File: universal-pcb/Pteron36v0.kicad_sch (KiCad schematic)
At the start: 64 parts, among them J1 AudioJack4, J2 AudioJack4, J3 Conn_01x04, SW10 SW_PUSH, SW12 SW_PUSH, SW13 SW_PUSH, SW14 SW_PUSH, SW15 SW_PUSH, SW17 SW_PUSH, SW18 SW_PUSH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

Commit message: super is ready
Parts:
- added LOGO? (x2): LOGO-OTL, personal-logo:peacock-medium, symbol SparkFun-Aesthetics:LOGO-OTL
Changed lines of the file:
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@@
+    )
+  )
+  (symbol (lib_id "SparkFun-Aesthetics:LOGO-OTL") (at 252.73 76.2 0) (unit 1)
+    (in_bom yes) (on_board yes)
+    (property "Reference" "LOGO?" (id 0) (at 252.73 76.2 0)
+      (effects (font (size 1.27 1.27)) hide)
+    )
+    (property "Value" "LOGO-OTL" (id 1) (at 252.73 76.2 0)
+      (effects (font (size 1.27 1.27)) hide)
+    )
+    (property "Footprint" "personal-logo:peacock-medium" (id 2) (at 253.492 72.39 0)
+      (effects (font (size 0.508 0.508)) hide)
+    )
+    (property "Datasheet" "" (id 3) (at 252.73 76.2 0)
+      (effects (font (size 1.27 1.27)) hide)
+    )
+  )
+  (symbol (lib_id "SparkFun-Aesthetics:LOGO-OTL") (at 252.73 86.36 0) (unit 1)
+    (in_bom yes) (on_board yes)
+    (property "Reference" "LOGO?" (id 0) (at 252.73 86.36 0)
+      (effects (font (size 1.27 1.27)) hide)
+    )
+    (property "Value" "LOGO-OTL" (id 1) (at 252.73 86.36 0)
+      (effects (font (size 1.27 1.27)) hide)
+    )
+    (property "Footprint" "personal-logo:peacock-medium" (id 2) (at 253.492 82.55 0)
+      (effects (font (size 0.508 0.508)) hide)
+    )
+    (property "Datasheet" "" (id 3) (at 252.73 86.36 0)
+      (effects (font (size 1.27 1.27)) hide)
     )
   )
@@
       (reference "LOGO2") (unit 1) (value "LOGO-OTL") (footprint "personal-logo:miryoku-kicad-small")
     )
+    (path "/a9b58b6f-e7ea-4927-95e3-e75d74487149"
+      (reference "LOGO?") (unit 1) (value "LOGO-OTL") (footprint "personal-logo:peacock-medium")
+    )
+    (path "/f6a143f1-2ae8-4506-91d2-2bed25c6d340"
+      (reference "LOGO?") (unit 1) (value "LOGO-OTL") (footprint "personal-logo:peacock-medium")
+    )
     (path "/00000000-0000-0000-0000-0000607d063e"

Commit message: verify gerber
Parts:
- gave numbers to parts that had none: 2
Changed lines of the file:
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@@
   (symbol (lib_id "SparkFun-Aesthetics:LOGO-OTL") (at 252.73 76.2 0) (unit 1)
     (in_bom yes) (on_board yes)
-    (property "Reference" "LOGO?" (id 0) (at 252.73 76.2 0)
+    (property "Reference" "LOGO3" (id 0) (at 252.73 76.2 0)
       (effects (font (size 1.27 1.27)) hide)
     )
@@
   (symbol (lib_id "SparkFun-Aesthetics:LOGO-OTL") (at 252.73 86.36 0) (unit 1)
     (in_bom yes) (on_board yes)
-    (property "Reference" "LOGO?" (id 0) (at 252.73 86.36 0)
+    (property "Reference" "LOGO4" (id 0) (at 252.73 86.36 0)
       (effects (font (size 1.27 1.27)) hide)
     )
@@
     )
     (path "/a9b58b6f-e7ea-4927-95e3-e75d74487149"
-      (reference "LOGO?") (unit 1) (value "LOGO-OTL") (footprint "personal-logo:peacock-medium")
+      (reference "LOGO3") (unit 1) (value "LOGO-OTL") (footprint "personal-logo:peacock-medium")
     )
     (path "/f6a143f1-2ae8-4506-91d2-2bed25c6d340"
-      (reference "LOGO?") (unit 1) (value "LOGO-OTL") (footprint "personal-logo:peacock-medium")
+      (reference "LOGO4") (unit 1) (value "LOGO-OTL") (footprint "personal-logo:peacock-medium")
     )
     (path "/00000000-0000-0000-0000-0000607d063e"

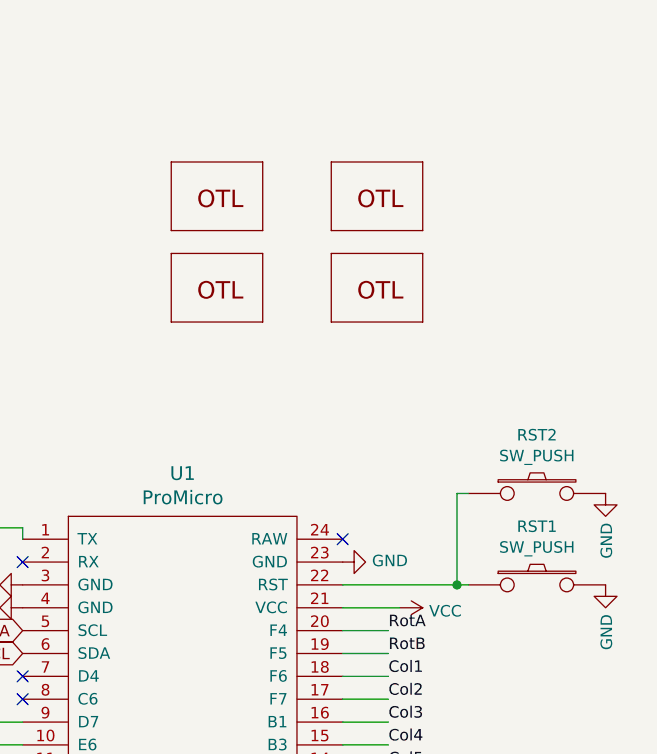
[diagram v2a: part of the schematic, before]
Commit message: introduce the snapable pcb with 4 config of keyboard possible
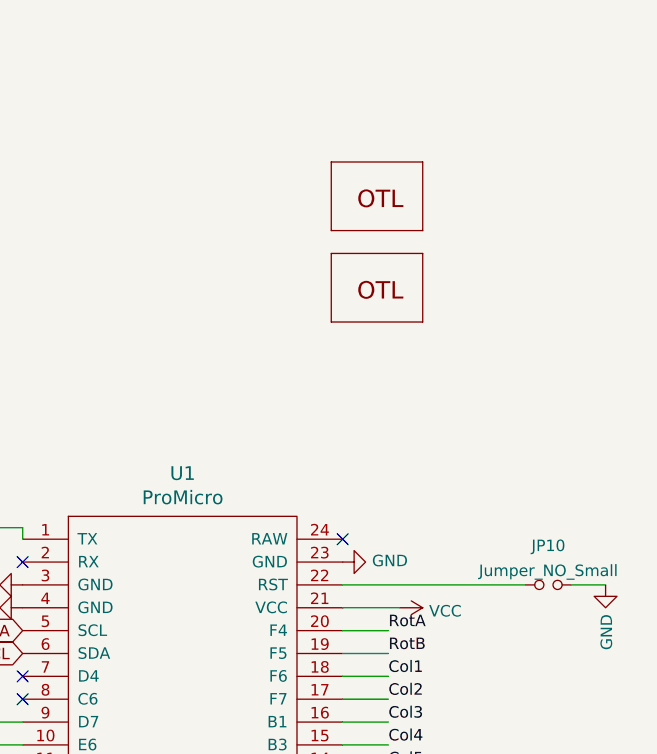
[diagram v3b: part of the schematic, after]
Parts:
- removed LOGO1, LOGO2: LOGO-OTL, personal-logo:miryoku-kicad-small, symbol SparkFun-Aesthetics:LOGO-OTL
- removed RST1, RST2: SW_PUSH, acheron_Hardware:smdPushBtn, symbol keyboard_parts:SW_PUSH
- added JP10: Jumper_NO_Small, User-Submitted:solder_jumper, symbol Device:Jumper_NO_Small
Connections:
- net GND: now also JP10.2
- net at U1.22 (RST): now also JP10.1
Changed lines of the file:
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@@
   (junction (at 107.95 152.4) (diameter 1.016) (color 0 0 0 0))
   (junction (at 119.38 77.47) (diameter 1.016) (color 0 0 0 0))
-  (junction (at 261.62 120.65) (diameter 1.016) (color 0 0 0 0))
   (no_connect (at 213.36 118.11))
   (no_connect (at 213.36 130.81))
@@
     (stroke (width 0) (type solid) (color 0 0 0 0))
   )
-  (wire (pts (xy 248.92 120.65) (xy 261.62 120.65))
+  (wire (pts (xy 248.92 120.65) (xy 269.24 120.65))
     (stroke (width 0) (type solid) (color 0 0 0 0))
   )
@@
     (stroke (width 0) (type solid) (color 0 0 0 0))
   )
-  (wire (pts (xy 261.62 110.49) (xy 262.89 110.49))
-    (stroke (width 0) (type solid) (color 0 0 0 0))
-  )
-  (wire (pts (xy 261.62 120.65) (xy 261.62 110.49))
-    (stroke (width 0) (type solid) (color 0 0 0 0))
-  )
-  (wire (pts (xy 261.62 120.65) (xy 262.89 120.65))
+  (wire (pts (xy 274.32 120.65) (xy 278.13 120.65))
     (stroke (width 0) (type solid) (color 0 0 0 0))
   )
@@
     (pin "2")
   )
+  (symbol (lib_id "Device:Jumper_NO_Small") (at 271.78 120.65 0) (unit 1)
+    (in_bom yes) (on_board yes) (fields_autoplaced)
+    (property "Reference" "JP10" (id 0) (at 271.78 116.3024 0))
+    (property "Value" "Jumper_NO_Small" (id 1) (at 271.78 119.0775 0))
+    (property "Footprint" "User-Submitted:solder_jumper" (id 2) (at 271.78 120.65 0)
+      (effects (font (size 1.27 1.27)) hide)
+    )
+    (property "Datasheet" "~" (id 3) (at 271.78 120.65 0)
+      (effects (font (size 1.27 1.27)) hide)
+    )
+    (pin "1")
+    (pin "2")
+  )
   (symbol (lib_id "power:GND") (at 83.82 144.78 270) (unit 1)
     (in_bom yes) (on_board yes)
@@
     )
     (property "Datasheet" "" (id 3) (at 248.92 118.11 0)
-      (effects (font (size 1.27 1.27)) hide)
-    )
-    (pin "1")
-  )
-  (symbol (lib_id "power:GND") (at 278.13 110.49 0) (unit 1)
-    (in_bom yes) (on_board yes)
-    (property "Reference" "#PWR0118" (id 0) (at 278.13 116.84 0)
-      (effects (font (size 1.27 1.27)) hide)
-    )
-    (property "Value" "GND" (id 1) (at 278.257 113.7412 90)
-      (effects (font (size 1.27 1.27)) (justify right))
-    )
-    (property "Footprint" "" (id 2) (at 278.13 110.49 0)
-      (effects (font (size 1.27 1.27)) hide)
-    )
-    (property "Datasheet" "" (id 3) (at 278.13 110.49 0)
       (effects (font (size 1.27 1.27)) hide)
     )
@@
     (pin "2")
   )
-  (symbol (lib_id "keyboard_parts:SW_PUSH") (at 270.51 110.49 0) (unit 1)
-    (in_bom yes) (on_board yes)
-    (property "Reference" "RST2" (id 0) (at 270.51 104.013 0))
-    (property "Value" "SW_PUSH" (id 1) (at 270.51 106.3244 0))
-    (property "Footprint" "acheron_Hardware:smdPushBtn" (id 2) (at 270.51 110.49 0)
-      (effects (font (size 1.524 1.524)) hide)
-    )
-    (property "Datasheet" "" (id 3) (at 270.51 110.49 0)
-      (effects (font (size 1.524 1.524)))
-    )
-    (pin "1")
-    (pin "2")
-  )
-  (symbol (lib_id "keyboard_parts:SW_PUSH") (at 270.51 120.65 0) (unit 1)
-    (in_bom yes) (on_board yes)
-    (property "Reference" "RST1" (id 0) (at 270.51 114.173 0))
-    (property "Value" "SW_PUSH" (id 1) (at 270.51 116.4844 0))
-    (property "Footprint" "acheron_Hardware:smdPushBtn" (id 2) (at 270.51 120.65 0)
-      (effects (font (size 1.524 1.524)) hide)
-    )
-    (property "Datasheet" "" (id 3) (at 270.51 120.65 0)
-      (effects (font (size 1.524 1.524)))
-    )
-    (pin "1")
-    (pin "2")
-  )
   (symbol (lib_id "Connector_Generic:Conn_01x03") (at 220.98 153.67 0) (unit 1)
     (in_bom yes) (on_board yes)
@@
     (pin "3")
     (pin "4")
-  )
-  (symbol (lib_id "SparkFun-Aesthetics:LOGO-OTL") (at 234.95 76.2 0) (unit 1)
-    (in_bom yes) (on_board yes)
-    (property "Reference" "LOGO1" (id 0) (at 234.95 76.2 0)
-      (effects (font (size 1.27 1.27)) hide)
-    )
-    (property "Value" "LOGO-OTL" (id 1) (at 234.95 76.2 0)
-      (effects (font (size 1.27 1.27)) hide)
-    )
-    (property "Footprint" "personal-logo:miryoku-kicad-small" (id 2) (at 235.712 72.39 0)
-      (effects (font (size 0.508 0.508)) hide)
-    )
-    (property "Datasheet" "" (id 3) (at 234.95 76.2 0)
-      (effects (font (size 1.27 1.27)) hide)
-    )
-  )
-  (symbol (lib_id "SparkFun-Aesthetics:LOGO-OTL") (at 234.95 86.36 0) (unit 1)
-    (in_bom yes) (on_board yes)
-    (property "Reference" "LOGO2" (id 0) (at 234.95 86.36 0)
-      (effects (font (size 1.27 1.27)) hide)
-    )
-    (property "Value" "LOGO-OTL" (id 1) (at 234.95 86.36 0)
-      (effects (font (size 1.27 1.27)) hide)
-    )
-    (property "Footprint" "personal-logo:miryoku-kicad-small" (id 2) (at 235.712 82.55 0)
-      (effects (font (size 0.508 0.508)) hide)
-    )
-    (property "Datasheet" "" (id 3) (at 234.95 86.36 0)
-      (effects (font (size 1.27 1.27)) hide)
-    )
   )
   (symbol (lib_id "SparkFun-Aesthetics:LOGO-OTL") (at 252.73 76.2 0) (unit 1)
@@
       (reference "#PWR0117") (unit 1) (value "VCC") (footprint "")
     )
-    (path "/00000000-0000-0000-0000-0000607e5c9b"
-      (reference "#PWR0118") (unit 1) (value "GND") (footprint "")
-    )
     (path "/00000000-0000-0000-0000-0000607efd8b"
       (reference "#PWR0119") (unit 1) (value "GND") (footprint "")
@@
       (reference "JP8") (unit 1) (value "Jumper_NO_Small") (footprint "SparkFun-Passives:PAD-JUMPER-2-NO_NO_SILK")
     )
-    (path "/00000000-0000-0000-0000-0000607a2bee"
-      (reference "LOGO1") (unit 1) (value "LOGO-OTL") (footprint "personal-logo:miryoku-kicad-small")
-    )
-    (path "/00000000-0000-0000-0000-0000607a2653"
-      (reference "LOGO2") (unit 1) (value "LOGO-OTL") (footprint "personal-logo:miryoku-kicad-small")
+    (path "/cf361c86-9d9b-4dea-a5c2-ea10f53cb6ec"
+      (reference "JP10") (unit 1) (value "Jumper_NO_Small") (footprint "User-Submitted:solder_jumper")
     )
     (path "/a9b58b6f-e7ea-4927-95e3-e75d74487149"
@@
       (reference "RE1") (unit 1) (value "Rotary_Encoder_Switch") (footprint "Rotary_Encoder:RotaryEncoder_Alps_EC11E-Switch_Vertical_H20mm")
     )
-    (path "/00000000-0000-0000-0000-0000607b81a2"
-      (reference "RST1") (unit 1) (value "SW_PUSH") (footprint "acheron_Hardware:smdPushBtn")
-    )
-    (path "/00000000-0000-0000-0000-0000607e0b2f"
-      (reference "RST2") (unit 1) (value "SW_PUSH") (footprint "acheron_Hardware:smdPushBtn")
-    )
     (path "/00000000-0000-0000-0000-000060963566"

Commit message: almost ready final super pcb
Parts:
- JP10: footprint User-Submitted:solder_jumper -> User-Submitted:SolderJumper-flip-2_P1.3mm_Open_Pad1.0x1.5mm
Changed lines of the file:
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@@
     (property "Reference" "JP10" (id 0) (at 271.78 116.3024 0))
     (property "Value" "Jumper_NO_Small" (id 1) (at 271.78 119.0775 0))
-    (property "Footprint" "User-Submitted:solder_jumper" (id 2) (at 271.78 120.65 0)
+    (property "Footprint" "User-Submitted:SolderJumper-flip-2_P1.3mm_Open_Pad1.0x1.5mm" (id 2) (at 271.78 120.65 0)
       (effects (font (size 1.27 1.27)) hide)
     )
@@
     )
     (path "/cf361c86-9d9b-4dea-a5c2-ea10f53cb6ec"
-      (reference "JP10") (unit 1) (value "Jumper_NO_Small") (footprint "User-Submitted:solder_jumper")
+      (reference "JP10") (unit 1) (value "Jumper_NO_Small") (footprint "User-Submitted:SolderJumper-flip-2_P1.3mm_Open_Pad1.0x1.5mm")
     )
     (path "/a9b58b6f-e7ea-4927-95e3-e75d74487149"

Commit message: updated pcb
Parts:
- H1, H2, H3, H4, H5, H6: footprint MountingHole:MountingHole_2.2mm_M2 -> MountingHole:MountingHole_2.2mm_M2_Pad
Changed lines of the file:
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@@
       (effects (font (size 1.27 1.27)) (justify left))
     )
-    (property "Footprint" "MountingHole:MountingHole_2.2mm_M2" (id 2) (at 127 167.64 0)
+    (property "Footprint" "MountingHole:MountingHole_2.2mm_M2_Pad" (id 2) (at 127 167.64 0)
       (effects (font (size 1.27 1.27)) hide)
     )
@@
       (effects (font (size 1.27 1.27)) (justify left))
     )
-    (property "Footprint" "MountingHole:MountingHole_2.2mm_M2" (id 2) (at 127 173.99 0)
+    (property "Footprint" "MountingHole:MountingHole_2.2mm_M2_Pad" (id 2) (at 127 173.99 0)
       (effects (font (size 1.27 1.27)) hide)
     )
@@
       (effects (font (size 1.27 1.27)) (justify left))
     )
-    (property "Footprint" "MountingHole:MountingHole_2.2mm_M2" (id 2) (at 133.35 167.64 0)
+    (property "Footprint" "MountingHole:MountingHole_2.2mm_M2_Pad" (id 2) (at 133.35 167.64 0)
       (effects (font (size 1.27 1.27)) hide)
     )
@@
       (effects (font (size 1.27 1.27)) (justify left))
     )
-    (property "Footprint" "MountingHole:MountingHole_2.2mm_M2" (id 2) (at 133.35 173.99 0)
+    (property "Footprint" "MountingHole:MountingHole_2.2mm_M2_Pad" (id 2) (at 133.35 173.99 0)
       (effects (font (size 1.27 1.27)) hide)
     )
@@
       (effects (font (size 1.27 1.27)) (justify left))
     )
-    (property "Footprint" "MountingHole:MountingHole_2.2mm_M2" (id 2) (at 139.7 167.64 0)
+    (property "Footprint" "MountingHole:MountingHole_2.2mm_M2_Pad" (id 2) (at 139.7 167.64 0)
       (effects (font (size 1.27 1.27)) hide)
     )
@@
       (effects (font (size 1.27 1.27)) (justify left))
     )
-    (property "Footprint" "MountingHole:MountingHole_2.2mm_M2" (id 2) (at 139.7 173.99 0)
+    (property "Footprint" "MountingHole:MountingHole_2.2mm_M2_Pad" (id 2) (at 139.7 173.99 0)
       (effects (font (size 1.27 1.27)) hide)
     )
@@
     )
     (path "/00000000-0000-0000-0000-000060e75eb4"
-      (reference "H1") (unit 1) (value "MountingHole") (footprint "MountingHole:MountingHole_2.2mm_M2")
+      (reference "H1") (unit 1) (value "MountingHole") (footprint "MountingHole:MountingHole_2.2mm_M2_Pad")
     )
     (path "/00000000-0000-0000-0000-000060e7da87"
-      (reference "H2") (unit 1) (value "MountingHole") (footprint "MountingHole:MountingHole_2.2mm_M2")
+      (reference "H2") (unit 1) (value "MountingHole") (footprint "MountingHole:MountingHole_2.2mm_M2_Pad")
     )
     (path "/00000000-0000-0000-0000-000060e77f07"
-      (reference "H3") (unit 1) (value "MountingHole") (footprint "MountingHole:MountingHole_2.2mm_M2")
+      (reference "H3") (unit 1) (value "MountingHole") (footprint "MountingHole:MountingHole_2.2mm_M2_Pad")
     )
     (path "/00000000-0000-0000-0000-000060e7e592"
-      (reference "H4") (unit 1) (value "MountingHole") (footprint "MountingHole:MountingHole_2.2mm_M2")
+      (reference "H4") (unit 1) (value "MountingHole") (footprint "MountingHole:MountingHole_2.2mm_M2_Pad")
     )
     (path "/00000000-0000-0000-0000-000060e7815c"
-      (reference "H5") (unit 1) (value "MountingHole") (footprint "MountingHole:MountingHole_2.2mm_M2")
+      (reference "H5") (unit 1) (value "MountingHole") (footprint "MountingHole:MountingHole_2.2mm_M2_Pad")
     )
     (path "/00000000-0000-0000-0000-000060e7e974"
-      (reference "H6") (unit 1) (value "MountingHole") (footprint "MountingHole:MountingHole_2.2mm_M2")
+      (reference "H6") (unit 1) (value "MountingHole") (footprint "MountingHole:MountingHole_2.2mm_M2_Pad")
     )
     (path "/00000000-0000-0000-0000-00006084e74f"
